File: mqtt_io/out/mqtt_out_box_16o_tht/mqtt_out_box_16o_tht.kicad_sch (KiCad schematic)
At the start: 106 parts, among them J1 Conn_01x04_Pin, J18 Conn_01x04_Pin, K1 FINDER-40.31, K10 FINDER-40.31, K11 FINDER-40.31, K12 FINDER-40.31, K13 FINDER-40.31, K14 FINDER-40.31, K15 FINDER-40.31, K16 FINDER-40.31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

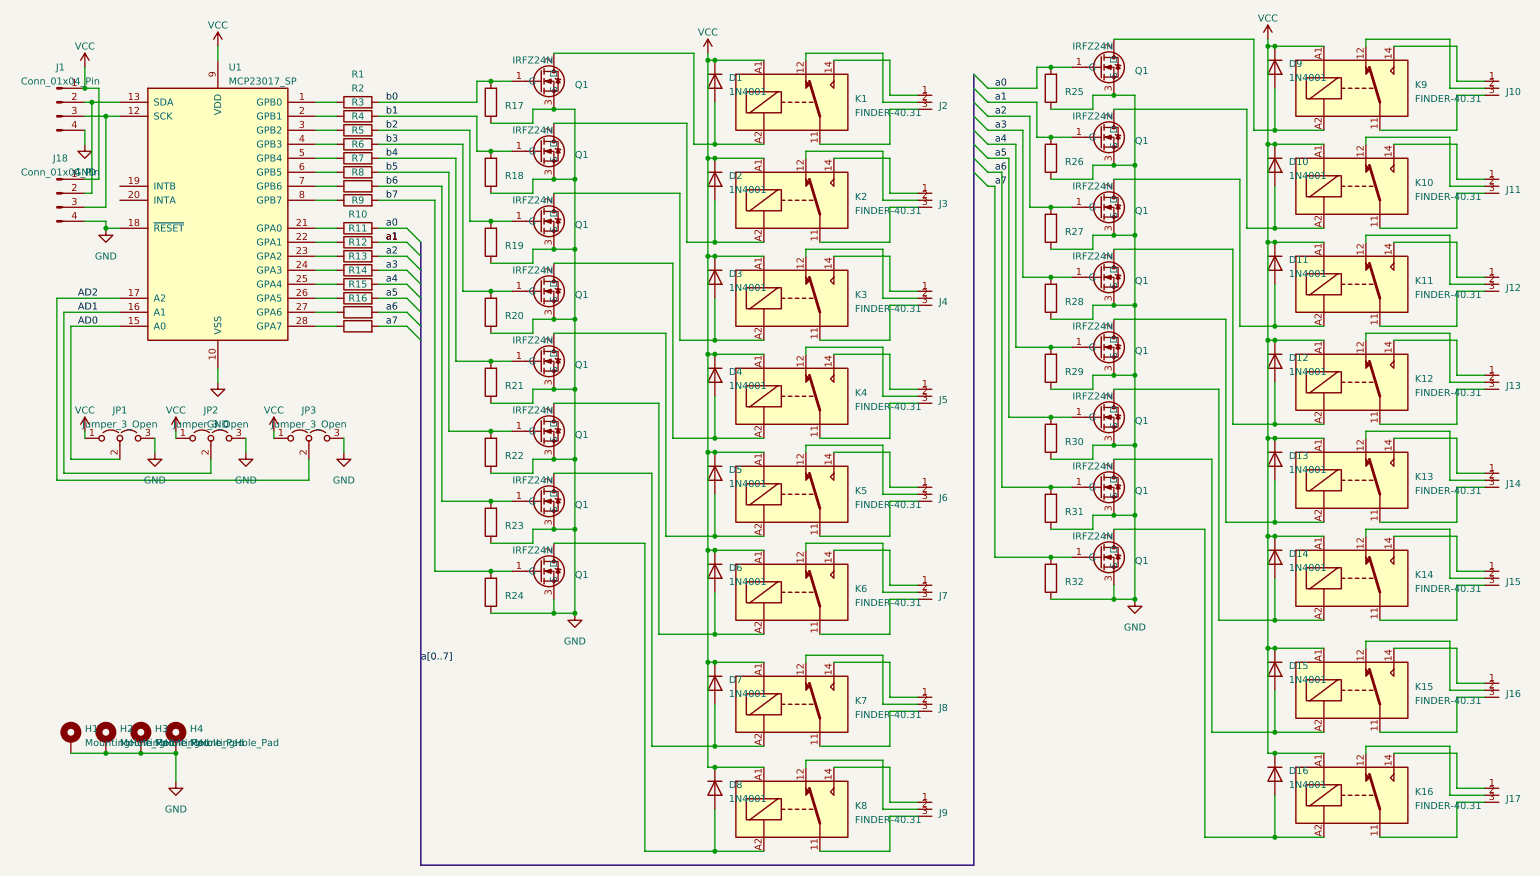
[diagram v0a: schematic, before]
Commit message: Pullup für ic2 eingefügt (4k7)
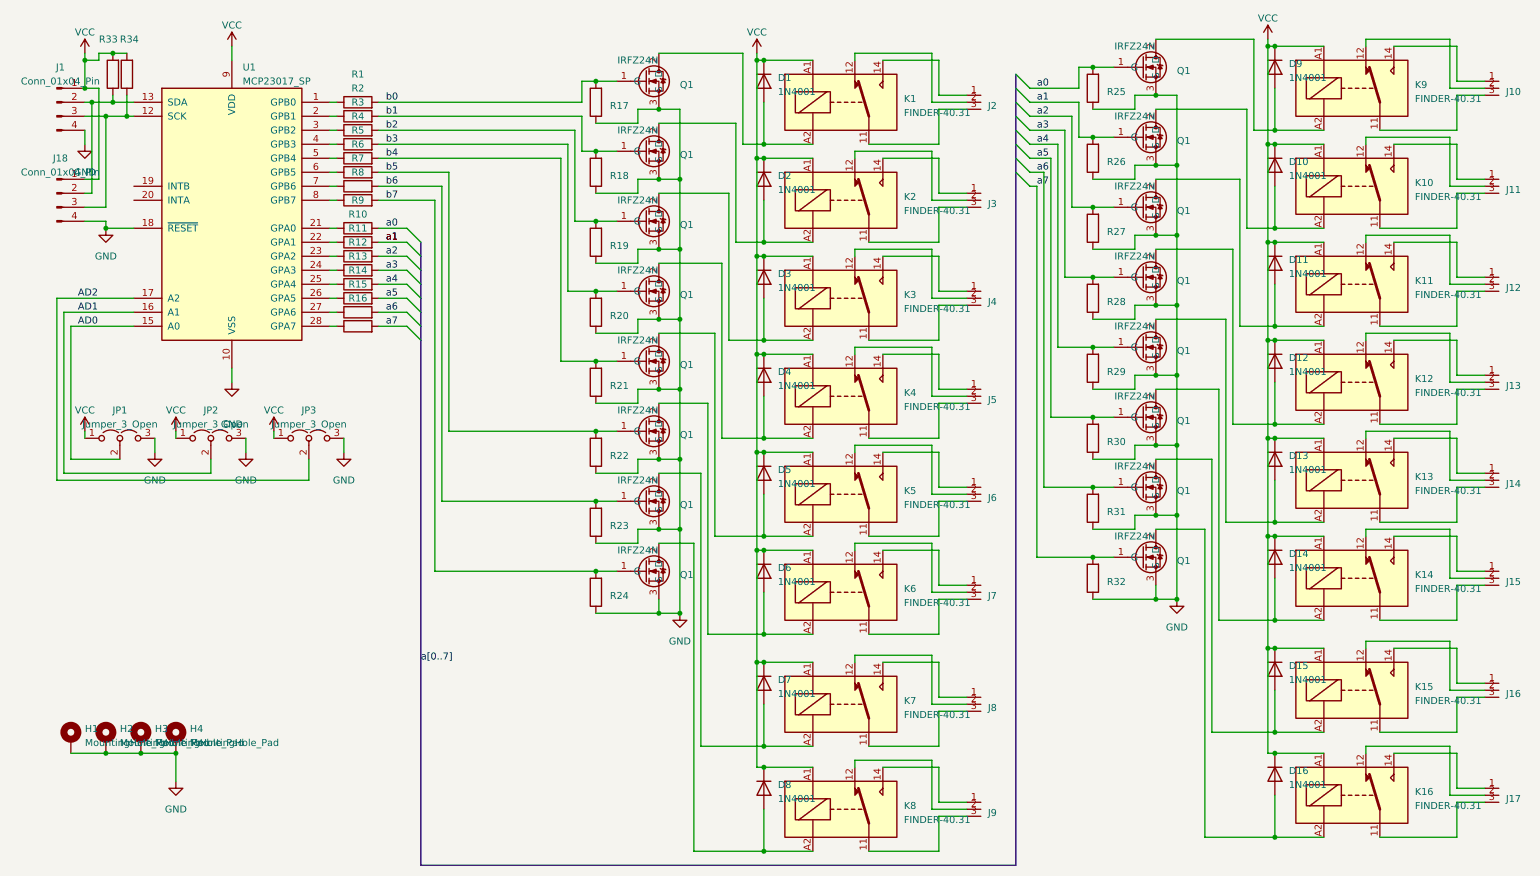
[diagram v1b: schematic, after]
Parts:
- added R33, R34: 4k7, Resistor_THT:R_Axial_DIN0204_L3.6mm_D1.6mm_P7.62mm_Horizontal, symbol Device:R
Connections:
- net VCC: now also R33.2, R34.2
- net at J1.3 (Pin_3), J18.3 (Pin_3), U1.12 (SCK): now also R34.1
- net at J1.2 (Pin_2), J18.2 (Pin_2), U1.13 (SDA): now also R33.1
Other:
- moved on the sheet: D1, D2, D3, D4, D5, D6, D7, D8, J2, J3, J4, J5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
